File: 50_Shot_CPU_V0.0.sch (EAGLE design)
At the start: 72 parts, among them IC1 PIC24FJ128GA010, IC2 93LC46ST, J1 J12, J12 A311422_nd, J13 22-23-2021, J14 22-23-2021, J3 22-23-2021, J4 22-23-2021, J5 22-23-2021, Q1 Qs5U34CT-ND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

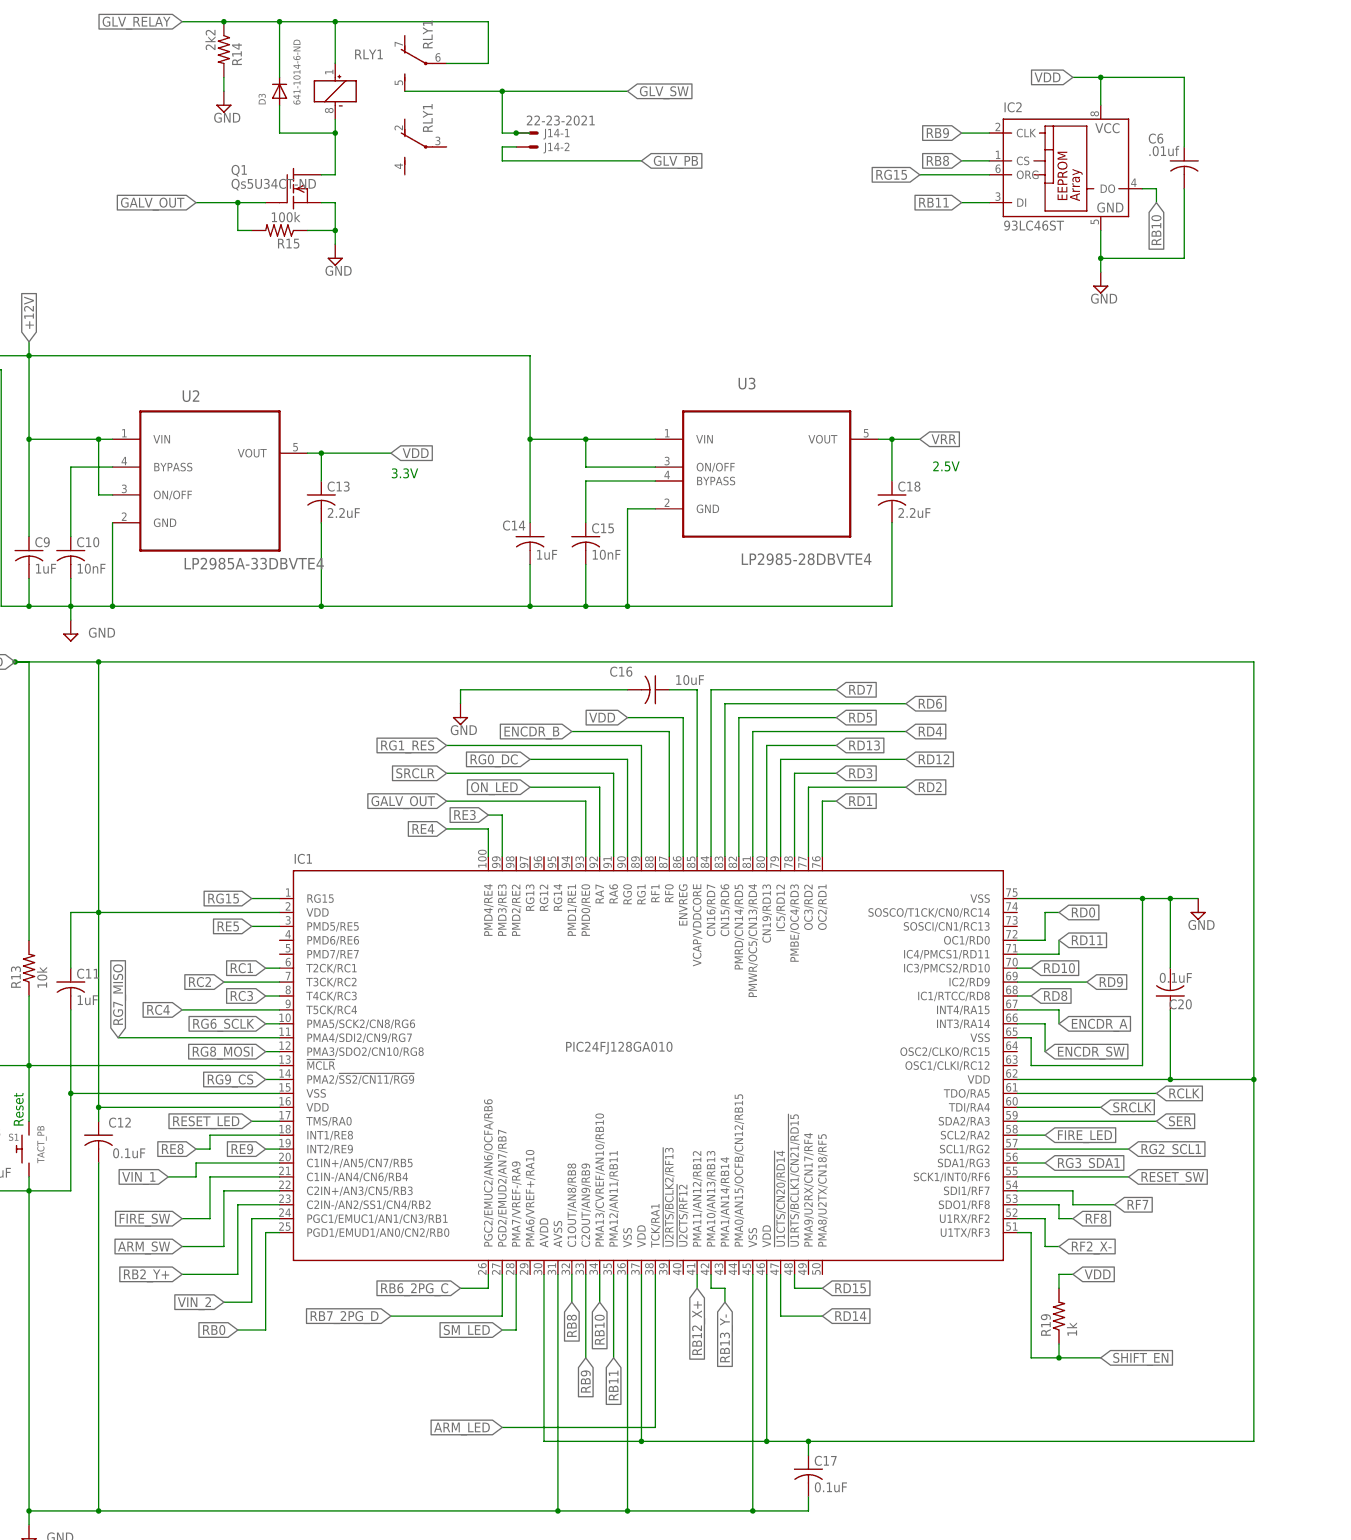
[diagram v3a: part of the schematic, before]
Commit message: Added parallel display header
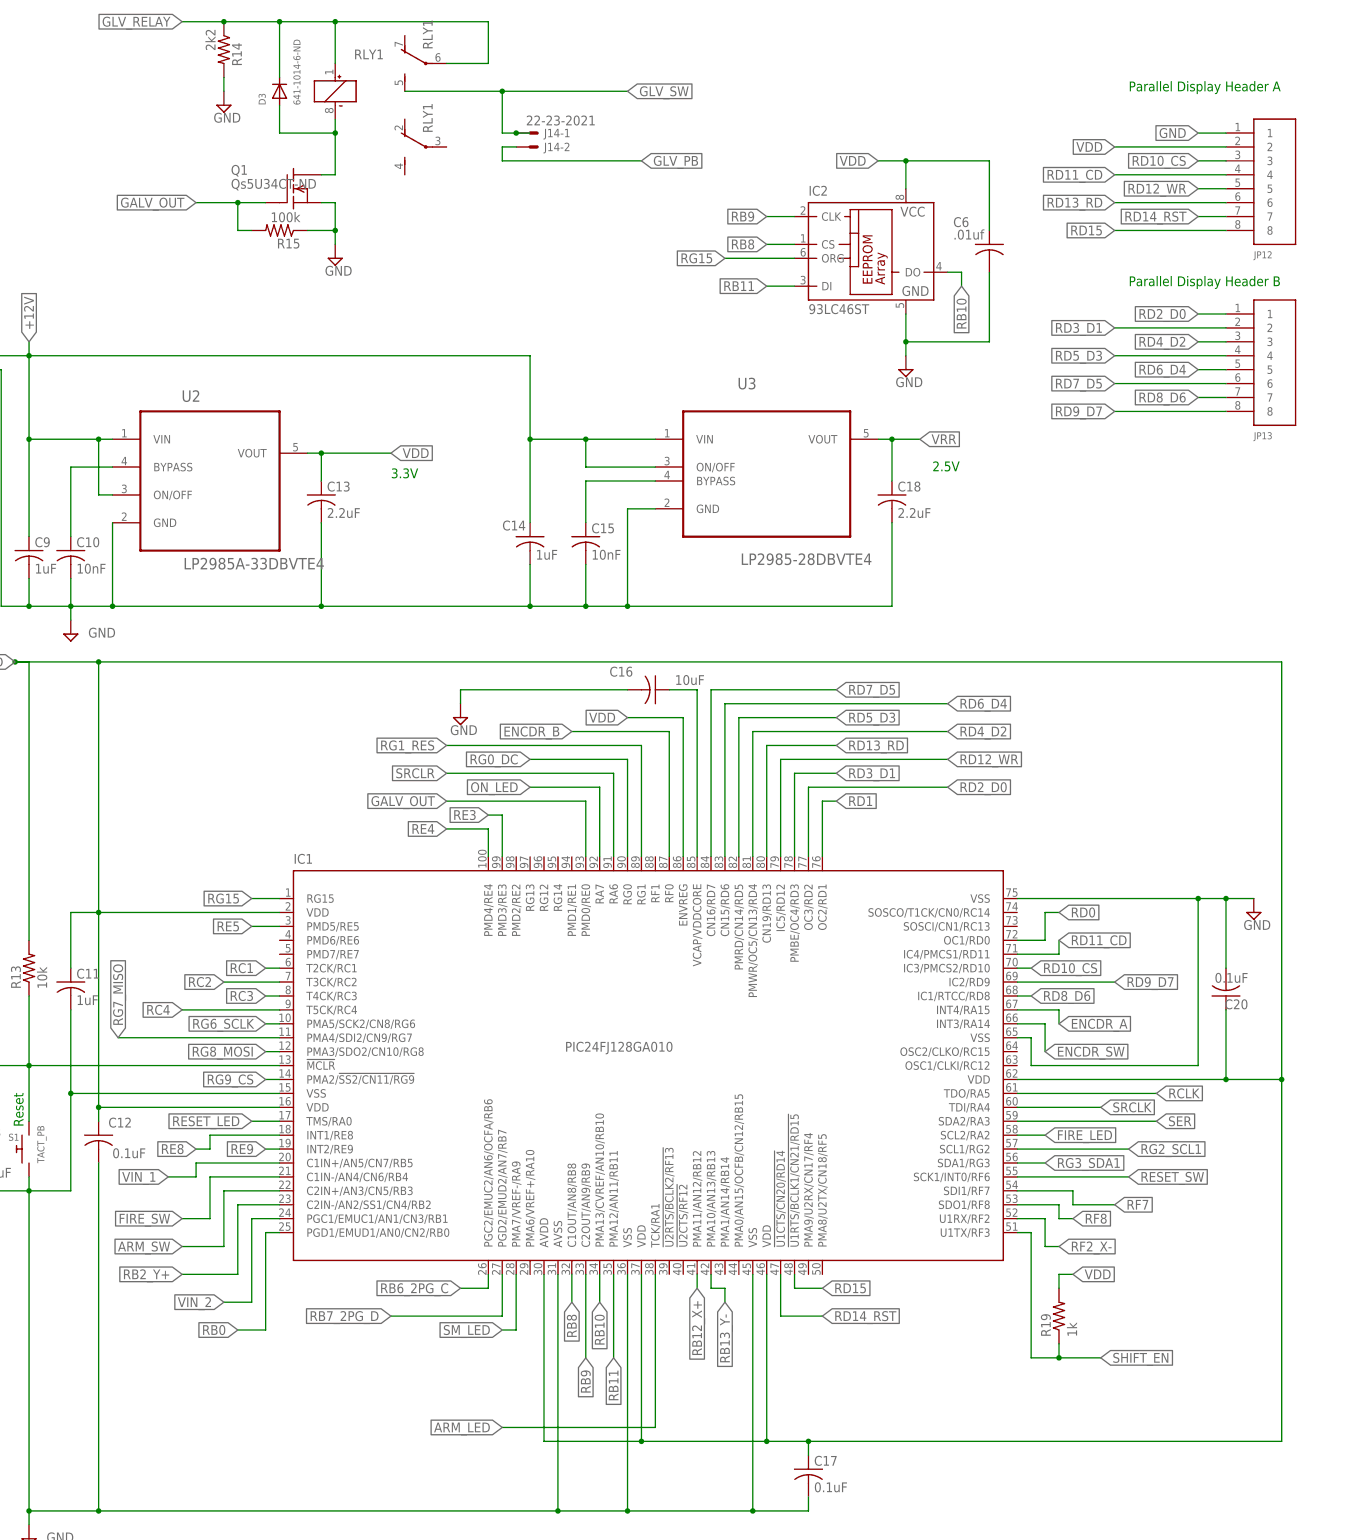
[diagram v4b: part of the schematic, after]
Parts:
- added JP12, JP13: SHERLOCK_8PIN_RGT, Mine:SHERLOCK_8PIN_RGT
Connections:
- removed net RD10: IC1.IC3/PMCS2/RD10
- removed net RD11: IC1.IC4/PMCS1/RD11
- removed net RD12: IC1.IC5/RD12
- removed net RD13: IC1.CN19/RD13
- removed net RD14: IC1.!U1CTS/CN20/RD14
- removed net RD2: IC1.OC3/RD2
- removed net RD3: IC1.PMBE/OC4/RD3
- removed net RD4: IC1.PMWR/OC5/CN13/RD4
- removed net RD5: IC1.PMRD/CN14/RD5
- removed net RD6: IC1.CN15/RD6
- removed net RD7: IC1.CN16/RD7
- removed net RD8: IC1.IC1/RTCC/RD8
- removed net RD9: IC1.IC2/RD9
- new net RD10_CS: IC1.IC3/PMCS2/RD10, JP12.3
- new net RD11_CD: IC1.IC4/PMCS1/RD11, JP12.4
- new net RD12_WR: IC1.IC5/RD12, JP12.5
- new net RD13_RD: IC1.CN19/RD13, JP12.6
- new net RD14_RST: IC1.!U1CTS/CN20/RD14, JP12.7
- new net RD2_D0: IC1.OC3/RD2, JP13.1
- new net RD3_D1: IC1.PMBE/OC4/RD3, JP13.2
- new net RD4_D2: IC1.PMWR/OC5/CN13/RD4, JP13.3
- new net RD5_D3: IC1.PMRD/CN14/RD5, JP13.4
- new net RD6_D4: IC1.CN15/RD6, JP13.5
- new net RD7_D5: IC1.CN16/RD7, JP13.6
- new net RD8_D6: IC1.IC1/RTCC/RD8, JP13.7
- new net RD9_D7: IC1.IC2/RD9, JP13.8
- net GND: now also JP12.1
- net RD15: now also JP12.8
- net VDD: now also JP12.2
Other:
- note added: "Parallel Display Header A"
- note added: "Parallel Display Header B"
- moved on the sheet: C20, C6, IC2

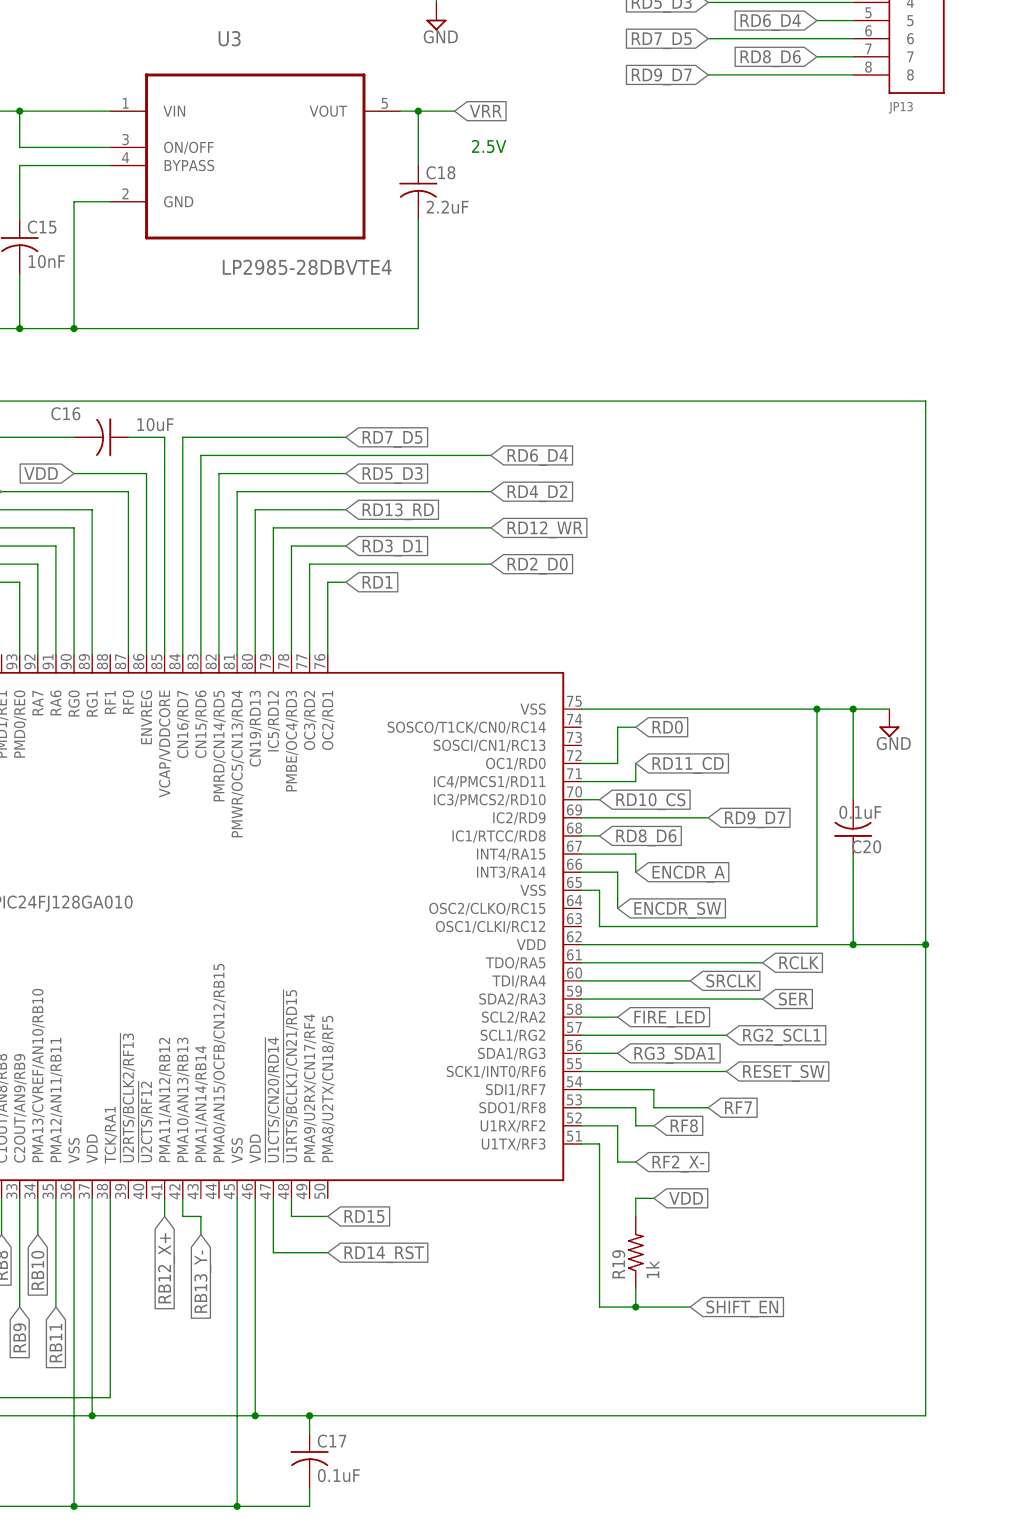
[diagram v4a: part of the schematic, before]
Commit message: Added UART Header
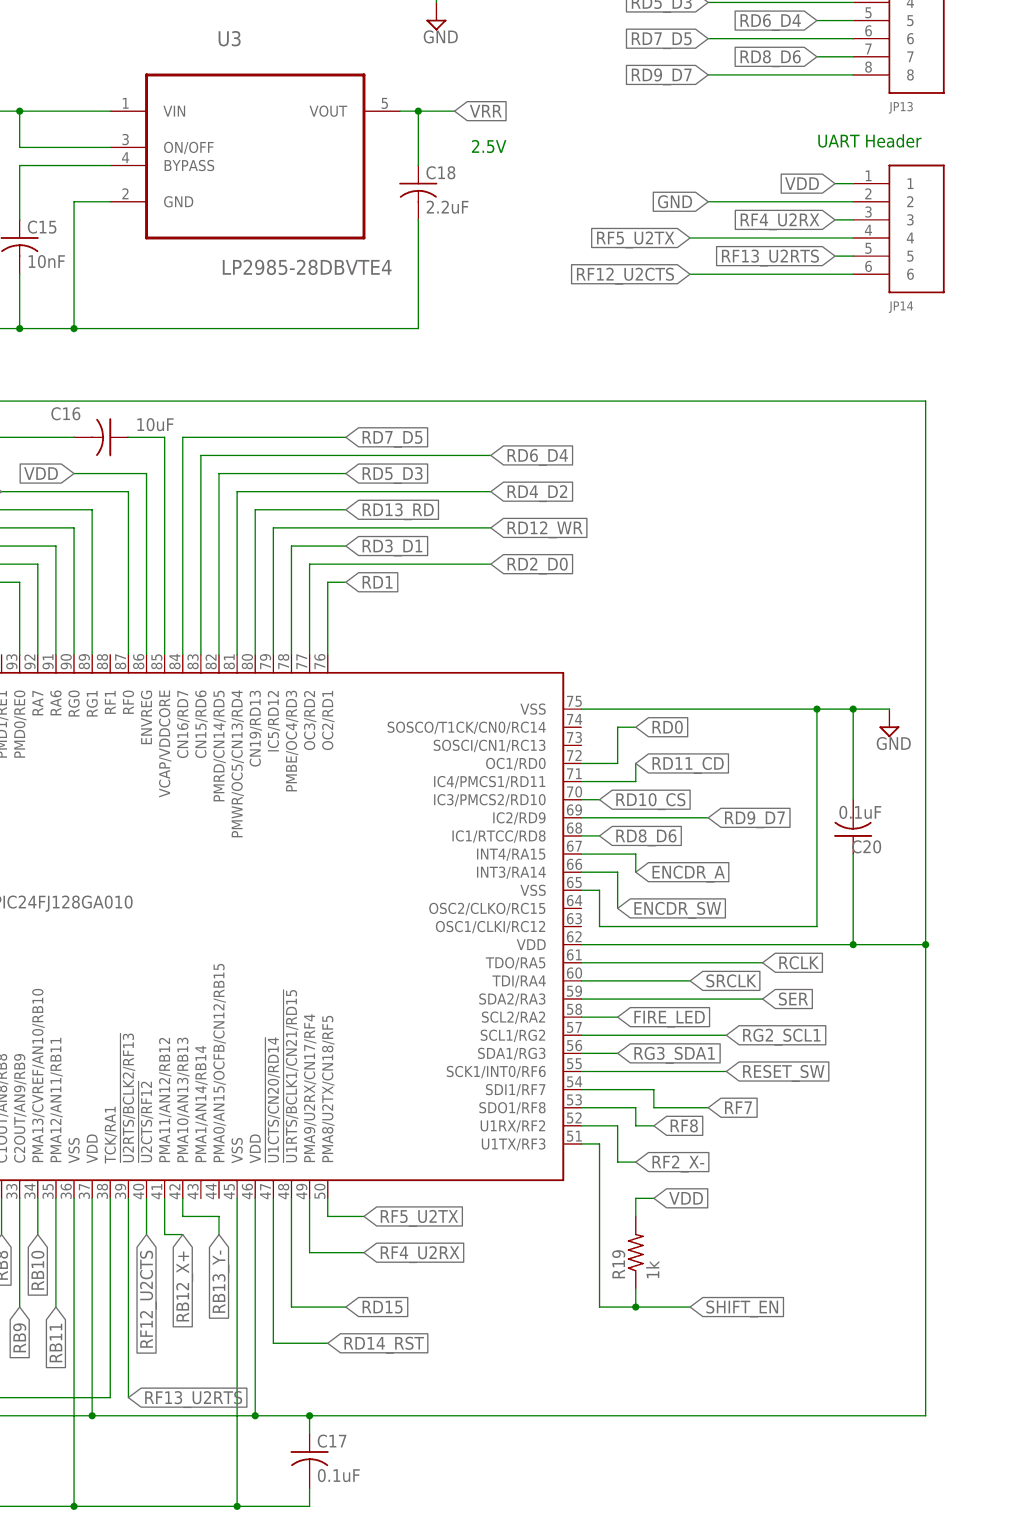
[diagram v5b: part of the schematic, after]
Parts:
- added JP14: SHERLOCK_6PIN_RGT, Mine:SHERLOCK_6PIN_RGT
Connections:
- new net RF12_U2CTS: IC1.!U2CTS/RF12, JP14.6
- new net RF13_U2RTS: IC1.!U2RTS/BCLK2/RF13, JP14.5
- new net RF4_U2RX: IC1.PMA9/U2RX/CN17/RF4, JP14.3
- new net RF5_U2TX: IC1.PMA8/U2TX/CN18/RF5, JP14.4
- net GND: now also JP14.2
- net VDD: now also JP14.1
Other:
- note added: "UART Header"
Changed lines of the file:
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@@
 <part name="JP12" library="Mine" deviceset="SHERLOCK_8PIN_RGT" device=""/>
 <part name="JP13" library="Mine" deviceset="SHERLOCK_8PIN_RGT" device=""/>
+<part name="JP14" library="Mine" deviceset="SHERLOCK_6PIN_RGT" device=""/>
 </parts>
 <sheets>
@@
 <text x="215.9" y="198.12" size="1.778" layer="91">Parallel Display Header A</text>
 <text x="215.9" y="162.56" size="1.778" layer="91">Parallel Display Header B</text>
+<text x="228.6" y="129.54" size="1.778" layer="91">UART Header</text>
 </plain>
 <instances>
@@
 <instance part="JP12" gate="G$1" x="238.76" y="180.34"/>
 <instance part="JP13" gate="G$1" x="238.76" y="147.32"/>
+<instance part="JP14" gate="G$1" x="238.76" y="119.38"/>
 </instances>
 <busses>
@@
 <label x="228.6" y="190.5" size="1.778" layer="95" rot="R180" xref="yes"/>
 </segment>
+<segment>
+<pinref part="JP14" gate="G$1" pin="2"/>
+<wire x1="233.68" y1="121.92" x2="213.36" y2="121.92" width="0.1524" layer="91"/>
+<label x="213.36" y="121.92" size="1.778" layer="95" rot="R180" xref="yes"/>
+</segment>
 </net>
 <net name="VDD" class="0">
@@
 <label x="213.36" y="187.96" size="1.778" layer="95" rot="R180" xref="yes"/>
 </segment>
+<segment>
+<pinref part="JP14" gate="G$1" pin="1"/>
+<wire x1="233.68" y1="124.46" x2="231.14" y2="124.46" width="0.1524" layer="91"/>
+<label x="231.14" y="124.46" size="1.778" layer="95" rot="R180" xref="yes"/>
+</segment>
 </net>
 <net name="SM_LED" class="0">
@@
 <segment>
 <pinref part="IC1" gate="G$1" pin="!U1RTS/BCLK1/CN21/RD15"/>
-<wire x1="154.94" y1="-17.78" x2="154.94" y2="-20.32" width="0.1524" layer="91"/>
-<wire x1="154.94" y1="-20.32" x2="160.02" y2="-20.32" width="0.1524" layer="91"/>
-<label x="160.02" y="-20.32" size="1.778" layer="95" xref="yes"/>
+<wire x1="154.94" y1="-17.78" x2="154.94" y2="-33.02" width="0.1524" layer="91"/>
+<wire x1="154.94" y1="-33.02" x2="162.56" y2="-33.02" width="0.1524" layer="91"/>
+<label x="162.56" y="-33.02" size="1.778" layer="95" xref="yes"/>
 </segment>
 <segment>
@@
 <segment>
 <pinref part="IC1" gate="G$1" pin="!U1CTS/CN20/RD14"/>
-<wire x1="152.4" y1="-17.78" x2="152.4" y2="-25.4" width="0.1524" layer="91"/>
-<wire x1="152.4" y1="-25.4" x2="160.02" y2="-25.4" width="0.1524" layer="91"/>
-<label x="160.02" y="-25.4" size="1.778" layer="95" xref="yes"/>
+<wire x1="152.4" y1="-17.78" x2="152.4" y2="-38.1" width="0.1524" layer="91"/>
+<wire x1="152.4" y1="-38.1" x2="160.02" y2="-38.1" width="0.1524" layer="91"/>
+<label x="160.02" y="-38.1" size="1.778" layer="95" xref="yes"/>
 </segment>
 <segment>
@@
 <segment>
 <pinref part="IC1" gate="G$1" pin="PMA11/AN12/RB12"/>
-<wire x1="137.16" y1="-17.78" x2="137.16" y2="-20.32" width="0.1524" layer="91"/>
-<label x="137.16" y="-20.32" size="1.778" layer="95" rot="R270" xref="yes"/>
+<wire x1="137.16" y1="-17.78" x2="137.16" y2="-22.86" width="0.1524" layer="91"/>
+<wire x1="137.16" y1="-22.86" x2="139.7" y2="-22.86" width="0.1524" layer="91"/>
+<label x="139.7" y="-22.86" size="1.778" layer="95" rot="R270" xref="yes"/>
 </segment>
 </net>
@@
 <pinref part="IC1" gate="G$1" pin="PMA10/AN13/RB13"/>
 <wire x1="139.7" y1="-17.78" x2="139.7" y2="-20.32" width="0.1524" layer="91"/>
-<wire x1="139.7" y1="-20.32" x2="142.24" y2="-20.32" width="0.1524" layer="91"/>
-<wire x1="142.24" y1="-20.32" x2="142.24" y2="-22.86" width="0.1524" layer="91"/>
-<label x="142.24" y="-22.86" size="1.778" layer="95" rot="R270" xref="yes"/>
+<wire x1="139.7" y1="-20.32" x2="144.78" y2="-20.32" width="0.1524" layer="91"/>
+<wire x1="144.78" y1="-20.32" x2="144.78" y2="-22.86" width="0.1524" layer="91"/>
+<label x="144.78" y="-22.86" size="1.778" layer="95" rot="R270" xref="yes"/>
 </segment>
 </net>
@@
 </segment>
 </net>
+<net name="RF13_U2RTS" class="0">
+<segment>
+<pinref part="JP14" gate="G$1" pin="5"/>
+<wire x1="233.68" y1="114.3" x2="231.14" y2="114.3" width="0.1524" layer="91"/>
+<label x="231.14" y="114.3" size="1.778" layer="95" rot="R180" xref="yes"/>
+</segment>
+<segment>
+<pinref part="IC1" gate="G$1" pin="!U2RTS/BCLK2/RF13"/>
+<wire x1="132.08" y1="-17.78" x2="132.08" y2="-45.72" width="0.1524" layer="91"/>
+<label x="132.08" y="-45.72" size="1.778" layer="95" xref="yes"/>
+</segment>
+</net>
+<net name="RF12_U2CTS" class="0">
+<segment>
+<pinref part="JP14" gate="G$1" pin="6"/>
+<wire x1="233.68" y1="111.76" x2="210.82" y2="111.76" width="0.1524" layer="91"/>
+<label x="210.82" y="111.76" size="1.778" layer="95" rot="R180" xref="yes"/>
+</segment>
+<segment>
+<pinref part="IC1" gate="G$1" pin="!U2CTS/RF12"/>
+<wire x1="134.62" y1="-17.78" x2="134.62" y2="-22.86" width="0.1524" layer="91"/>
+<label x="134.62" y="-22.86" size="1.778" layer="95" rot="R270" xref="yes"/>
+</segment>
+</net>
+<net name="RF5_U2TX" class="0">
+<segment>
+<pinref part="IC1" gate="G$1" pin="PMA8/U2TX/CN18/RF5"/>
+<wire x1="160.02" y1="-17.78" x2="160.02" y2="-20.32" width="0.1524" layer="91"/>
+<wire x1="160.02" y1="-20.32" x2="165.1" y2="-20.32" width="0.1524" layer="91"/>
+<label x="165.1" y="-20.32" size="1.778" layer="95" xref="yes"/>
+</segment>
+<segment>
+<pinref part="JP14" gate="G$1" pin="4"/>
+<wire x1="233.68" y1="116.84" x2="210.82" y2="116.84" width="0.1524" layer="91"/>
+<label x="210.82" y="116.84" size="1.778" layer="95" rot="R180" xref="yes"/>
+</segment>
+</net>
+<net name="RF4_U2RX" class="0">
+<segment>
+<pinref part="IC1" gate="G$1" pin="PMA9/U2RX/CN17/RF4"/>
+<wire x1="157.48" y1="-17.78" x2="157.48" y2="-25.4" width="0.1524" layer="91"/>
+<wire x1="157.48" y1="-25.4" x2="165.1" y2="-25.4" width="0.1524" layer="91"/>
+<label x="165.1" y="-25.4" size="1.778" layer="95" xref="yes"/>
+</segment>
+<segment>
+<pinref part="JP14" gate="G$1" pin="3"/>
+<wire x1="233.68" y1="119.38" x2="231.14" y2="119.38" width="0.1524" layer="91"/>
+<label x="231.14" y="119.38" size="1.778" layer="95" rot="R180" xref="yes"/>
+</segment>
+</net>
